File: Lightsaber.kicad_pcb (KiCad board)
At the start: 2 copper layers, 87.6 x 38.7 mm, 32 parts, among them J1 Neopixel LEDs, J2 USB_B_Micro, M1 Motor_DC, Q1 2N2222, Q2 2N3904, Q3 2N3904, SW1 SW_Push, SW2 SW_DIP_x01, U1 PAM8403D, U2 MPU-6050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

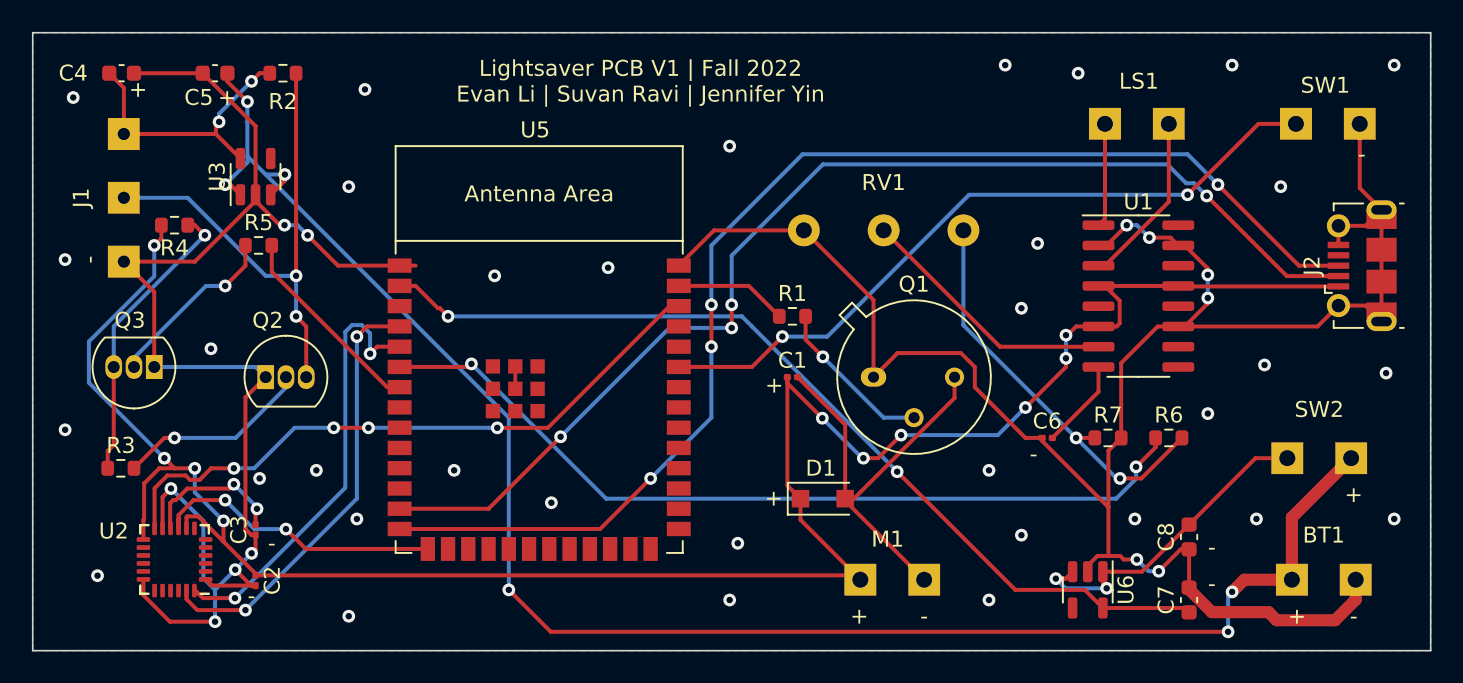
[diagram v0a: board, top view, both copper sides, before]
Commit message: thickened power traces, fixed all errors, placed test points on layout
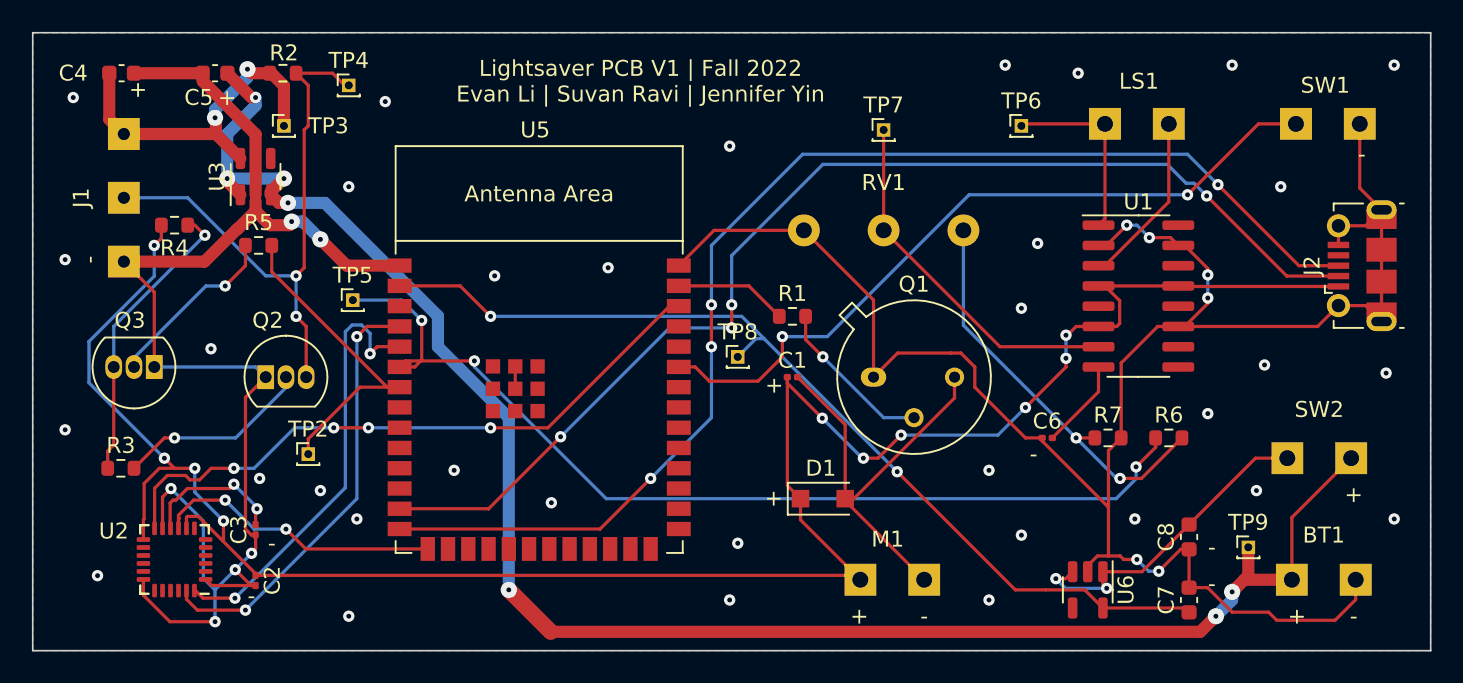
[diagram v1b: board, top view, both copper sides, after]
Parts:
- added TP2: TestPoint, Connector_PinHeader_1.00mm:PinHeader_1x01_P1.00mm_Vertical, F.Cu at (118.9, 105.2)
- added TP3: TestPoint, Connector_PinHeader_1.00mm:PinHeader_1x01_P1.00mm_Vertical, F.Cu at (117.3, 84.6)
- added TP4: TestPoint, Connector_PinHeader_1.00mm:PinHeader_1x01_P1.00mm_Vertical, F.Cu at (121.4, 82.0)
- added TP5: TestPoint, Connector_PinHeader_1.00mm:PinHeader_1x01_P1.00mm_Vertical, F.Cu at (121.7, 95.5)
- added TP6: TestPoint, Connector_PinHeader_1.00mm:PinHeader_1x01_P1.00mm_Vertical, F.Cu at (163.6, 84.6)
- added TP7: TestPoint, Connector_PinHeader_1.00mm:PinHeader_1x01_P1.00mm_Vertical, F.Cu at (154.9, 84.8)
- added TP8: TestPoint, Connector_PinHeader_1.00mm:PinHeader_1x01_P1.00mm_Vertical, F.Cu at (145.8, 99.1)
- added TP9: TestPoint, Connector_PinHeader_1.00mm:PinHeader_1x01_P1.00mm_Vertical, F.Cu at (177.8, 111.0)
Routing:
- net Net-(R6-Pad1): track 53.3 -> 62.6 mm, vias 2 -> 3
- net Net-(R5-Pad2): track 12.7 -> 20.7 mm
- net Net-(RV1-Pad2): track 16.5 -> 22.8 mm
- net Net-(LS1-Pad1): track 6.52 -> 11.8 mm
- net Net-(C4-Pad1): track 17.7 -> 22.3 mm
- net Net-(J1-Pad2): track 32.1 -> 36.4 mm
- net +9V: track 108.1 -> 110.3 mm, vias 6 -> 7
- net Net-(C7-Pad1): track 58.0 -> 60.1 mm
- net Net-(SW1-Pad1): track 45.0 -> 46.5 mm
- net GND: track 213.9 -> 213.2 mm

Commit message: finished
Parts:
- removed C2, C3: 0.1uF, Capacitor_SMD:C_0201_0603Metric
- removed U2: MPU-6050, Sensor_Motion:InvenSense_QFN-24_4x4mm_P0.5mm
- added J3: Conn_01x05_Female, Connector_PinSocket_2.54mm:PinSocket_1x05_P2.54mm_Vertical, F.Cu at (116.1, 114.8)
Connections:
- U5 pad 5: Net-(U2-Pad24) -> unconnected-(U5-Pad5)
- U5 pad 7: Net-(R5-Pad2) -> unconnected-(U5-Pad7)
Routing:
- net GND: track 213.2 -> 179.6 mm, vias 46 -> 39
- net Net-(U2-Pad24): track 27.5 -> 0.00 mm, vias 2 -> 0
- net Net-(C3-Pad2): track 9.29 -> 0.00 mm, vias 2 -> 0
- net +3.3V: track 137.0 -> 143.4 mm, vias 10 -> 14
- net Net-(U5-Pad38): track 40.3 -> 34.6 mm, vias 4 -> 1
- net Net-(U5-Pad15): track 18.8 -> 14.4 mm, vias 2 -> 0
- net Net-(U5-Pad4): track 27.5 -> 23.7 mm
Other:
- board text added: "CL"
- board text added: "DA"
- board text added: "INT"
